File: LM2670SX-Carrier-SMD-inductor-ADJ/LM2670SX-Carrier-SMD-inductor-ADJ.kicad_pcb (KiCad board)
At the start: 2 copper layers, 19.6 x 32.4 mm, 11 parts, among them IC1 LM2670SX-3.3_NOPB, J1 Conn_01x03

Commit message: updating and adding some more of these. sending off to fab.
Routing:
- net GND: track 17.1 -> 51.7 mm, vias 2 -> 1
- net Net-(J1-Pin_2): track 3.42 -> 28.3 mm
- net +VDC: track 4.90 -> 24.7 mm
- net +3V3: track 14.1 -> 0.00 mm
- net Net-(IC1-SWITCH_OUTPUT): track 3.00 -> 17.1 mm, vias 1 -> 2
- net Net-(R1-Pad2): track 0.00 -> 14.0 mm
- net Net-(IC1-FEEDBACK/FB): track 0.00 -> 13.7 mm

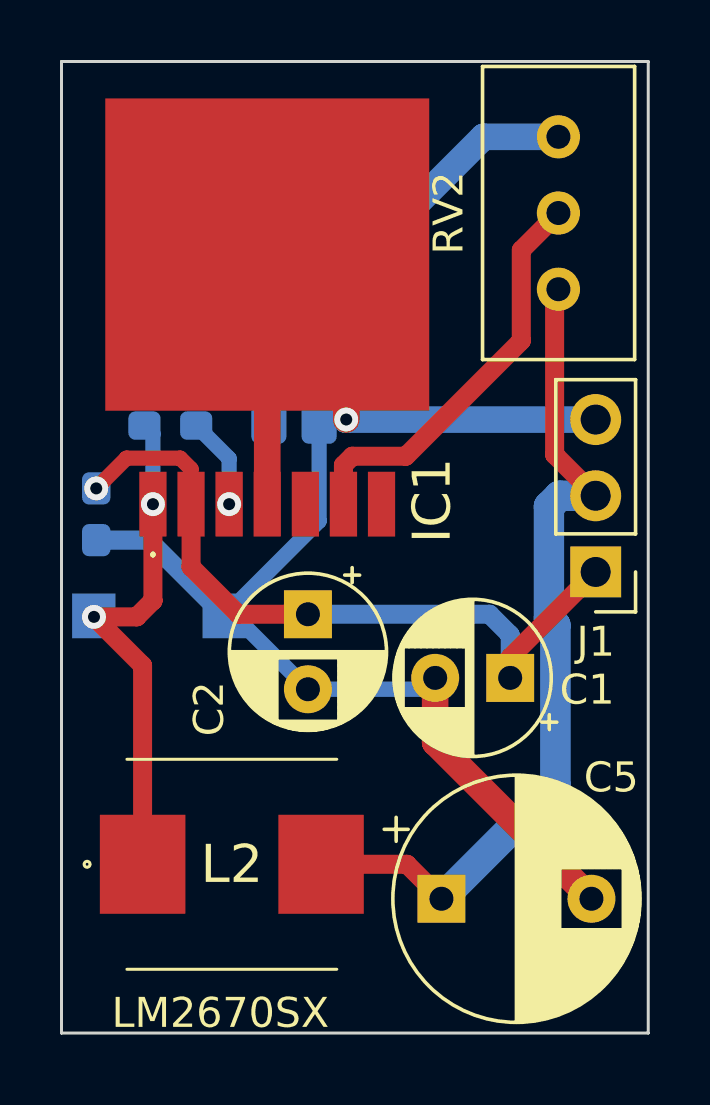
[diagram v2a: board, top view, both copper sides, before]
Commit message: adj smd inductor update
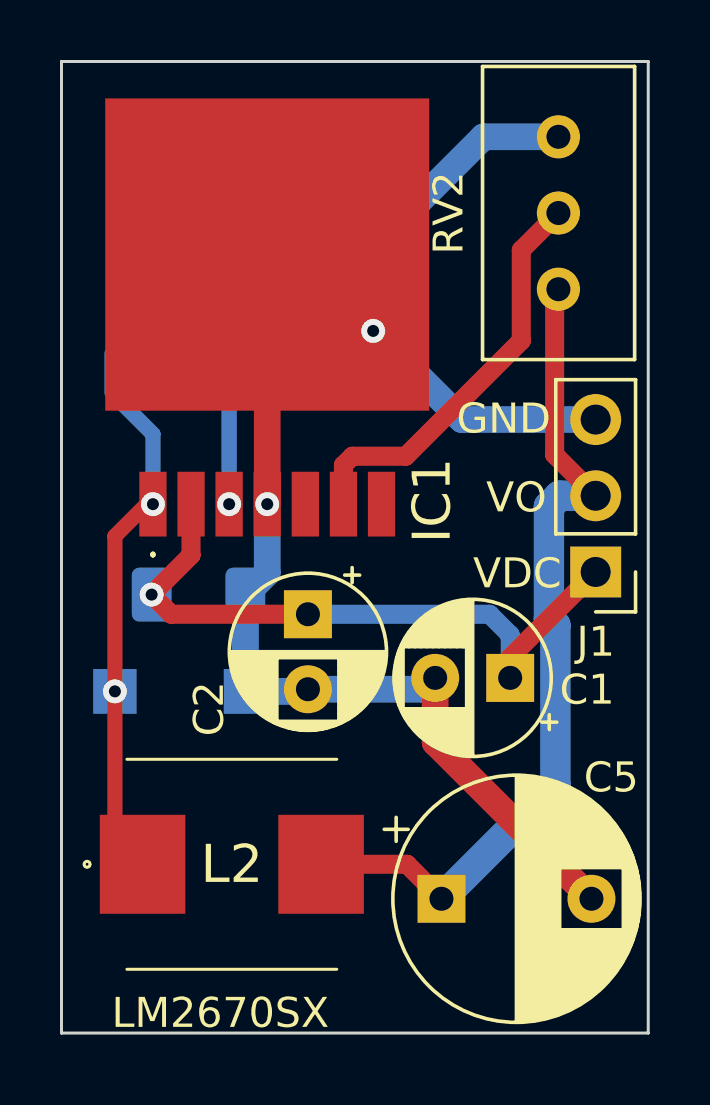
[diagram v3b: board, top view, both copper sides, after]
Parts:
- C3, C4: footprint Capacitor_SMD:C_0603_1608Metric_Pad1.08x0.95mm_HandSolder -> Capacitor_SMD:C_1206_3216Metric_Pad1.33x1.80mm_HandSolder
- R1: footprint Resistor_SMD:R_0612_1632Metric_Pad1.18x3.40mm_HandSolder -> Resistor_SMD:R_1206_3216Metric_Pad1.30x1.75mm_HandSolder
- moved C4 4.33 mm to (175.5, 102.2), turned to 0 degrees
- moved D2 2.61 mm to (174.9, 105.5)
- moved R1 2.33 mm to (179.8, 93.4)
- moved C3 1.76 mm to (174.6, 94.8)
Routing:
- net GND: track 51.7 -> 40.7 mm, vias 1 -> 2
- net +VDC: track 24.7 -> 22.2 mm
- net Net-(R1-Pad2): track 14.0 -> 12.0 mm
- net Net-(IC1-CBOOST/CB): track 3.07 -> 4.53 mm
- net Net-(IC1-SWITCH_OUTPUT): track 17.1 -> 17.8 mm
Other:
- board text added: "GND"
- board text added: "VDC"
- board text added: "VO"
